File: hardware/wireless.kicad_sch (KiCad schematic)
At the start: 1 part, among them U12 ESP32-C6-MINI-1/U

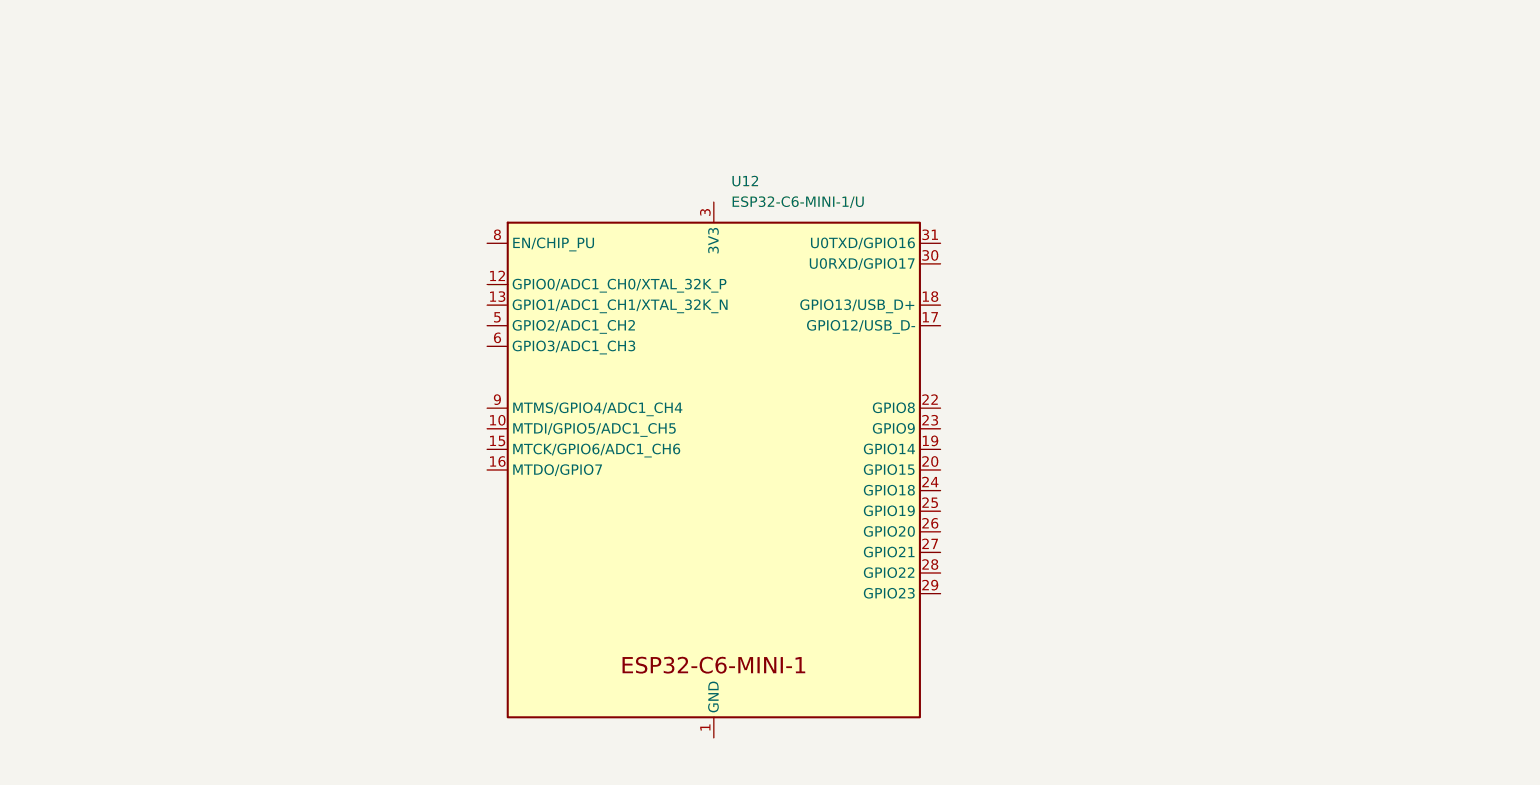
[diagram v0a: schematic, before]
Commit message: ✨ Done wireless schematic
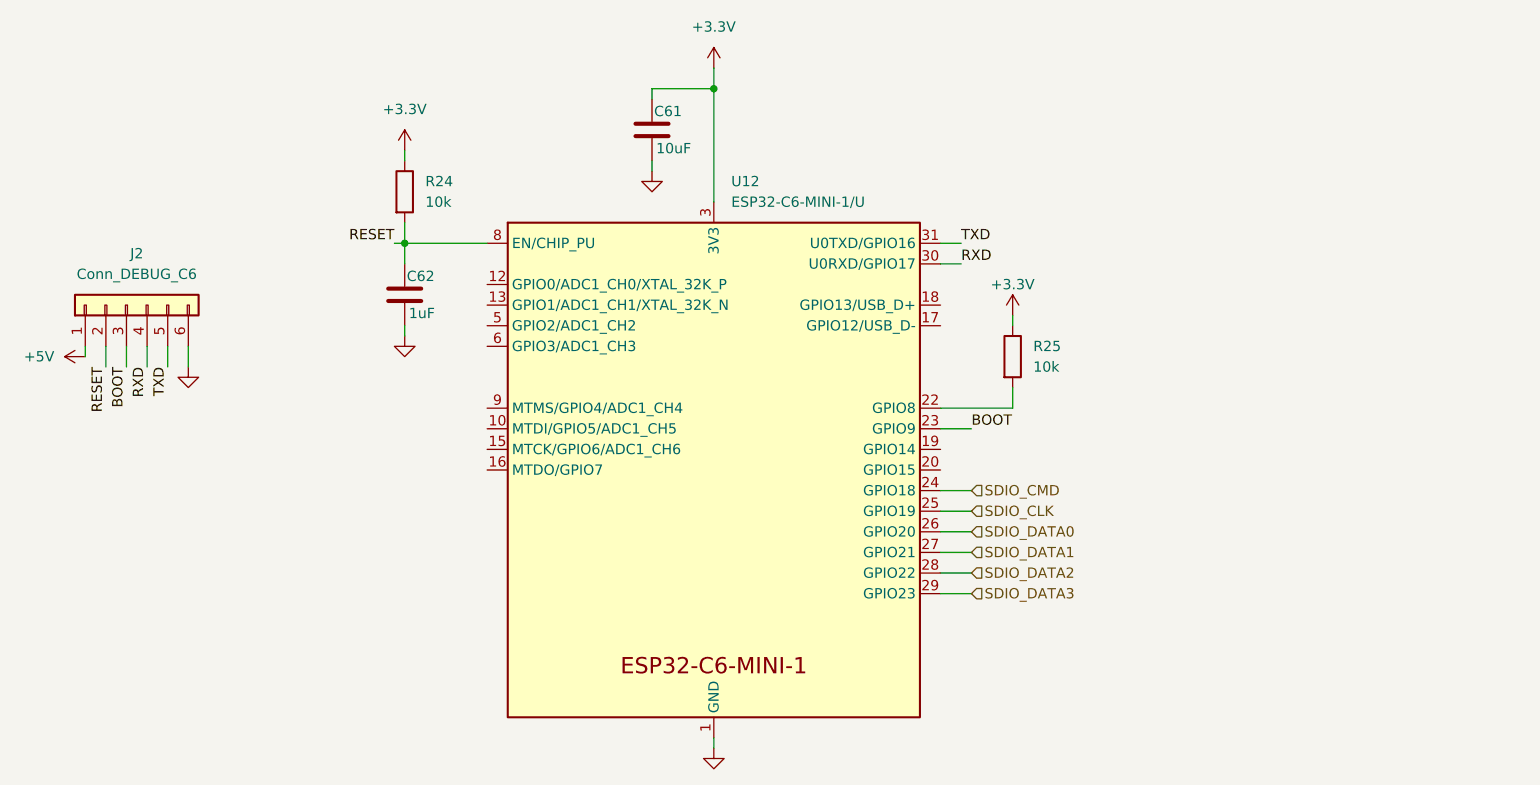
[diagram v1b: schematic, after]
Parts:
- added C61: 10uF, Capacitor_SMD:C_0805_2012Metric, symbol Device:C
- added C62: 1uF, Capacitor_SMD:C_0603_1608Metric, symbol Device:C
- added J2: Conn_DEBUG_C6, Connector_JST:JST_SHL_SM06B-SHLS-TF_1x06-1MP_P1.00mm_Horizontal, symbol Connector_Generic:Conn_01x06
- added R24, R25: 10k, PCM_Resistor_SMD_AKL:R_0603_1608Metric, symbol Device:R
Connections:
- net GND: now reaches U12.1 (GND), U12.11 (GND), U12.14 (GND), U12.2 (GND), U12.36 (GND), U12.37 (GND), U12.38 (GND), U12.39 (GND), U12.40 (GND), U12.41 (GND), U12.42 (GND), U12.43 (GND), U12.44 (GND), U12.45 (GND), U12.46 (GND), U12.47 (GND), U12.48 (GND), U12.49 (GND), U12.50 (GND), U12.51 (GND), U12.52 (GND), U12.53 (GND)
- net GND: now also C61.2, C62.2, J2.6 (Pin_6)
- net at U12.22 (GPIO8): now also R25.2
- net BOOT: now reaches U12.23 (GPIO9)
- net BOOT: now also J2.3 (Pin_3)
- net SDIO_CMD: now reaches U12.24 (GPIO18)
- net SDIO_CLK: now reaches U12.25 (GPIO19)
- net SDIO_DATA0: now reaches U12.26 (GPIO20)
- net SDIO_DATA1: now reaches U12.27 (GPIO21)
- net SDIO_DATA2: now reaches U12.28 (GPIO22)
- net SDIO_DATA3: now reaches U12.29 (GPIO23)
- net +3.3V: now reaches U12.3 (3V3)
- net +3.3V: now also C61.1, R24.1, R25.1
- net RXD: now reaches U12.30 (U0RXD/GPIO17)
- net RXD: now also J2.4 (Pin_4)
- net TXD: now reaches U12.31 (U0TXD/GPIO16)
- net TXD: now also J2.5 (Pin_5)
- net RESET: now reaches U12.8 (EN/CHIP_PU)
- net RESET: now also C62.1, J2.2 (Pin_2), R24.2
- new net +5V: J2.1 (Pin_1)

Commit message: 📂 PCB updates
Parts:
- added R30, R31, R32, R33, R34, R35: 51k, Resistor_SMD:R_0603_1608Metric, symbol Device:R
- C61: footprint Capacitor_SMD:C_0805_2012Metric -> Capacitor_SMD:C_0603_1608Metric
- R24, R25: footprint PCM_Resistor_SMD_AKL:R_0603_1608Metric -> Resistor_SMD:R_0603_1608Metric
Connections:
- net +3.3V: now also R30.2, R31.2, R32.2, R33.2, R34.2, R35.2
- net SDIO_CLK: now also R34.1
- net SDIO_CMD: now also R35.1
- net SDIO_DATA0: now also R30.1
- net SDIO_DATA1: now also R31.1
- net SDIO_DATA2: now also R32.1
- net SDIO_DATA3: now also R33.1
- net JTAG_DN: now reaches U12.17 (GPIO12/USB_D-)
- net JTAG_DN: now also J2.5 (Pin_5)
- net JTAG_DP: now reaches U12.18 (GPIO13/USB_D+)
- net JTAG_DP: now also J2.4 (Pin_4)
- net RXD: no longer names the net of U12.30 (U0RXD/GPIO17)
- net RXD: no longer J2.4 (Pin_4)
- net TXD: no longer names the net of U12.31 (U0TXD/GPIO16)
- net TXD: no longer J2.5 (Pin_5)
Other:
- moved on the sheet: R25

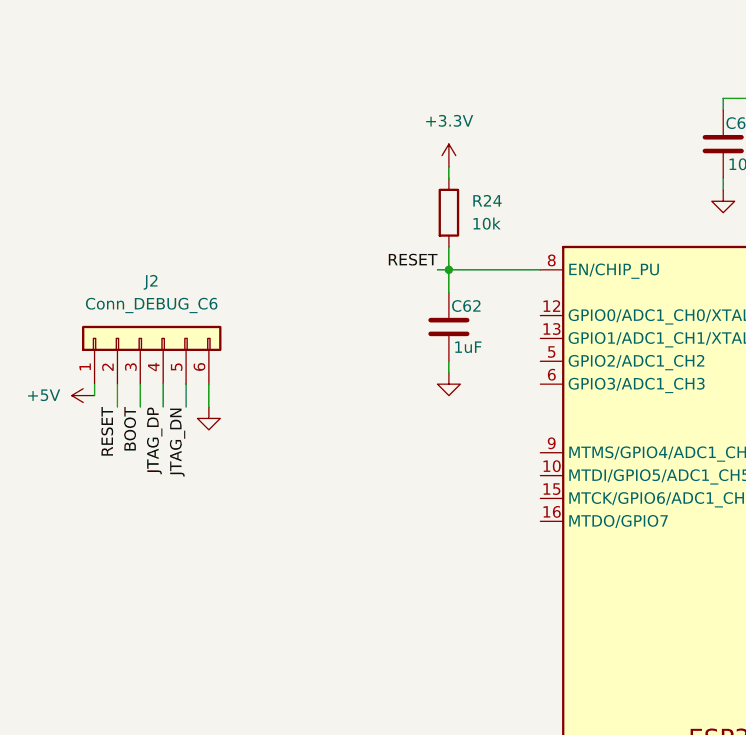
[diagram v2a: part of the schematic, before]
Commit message: 🐛 Fix errors from rev1.0
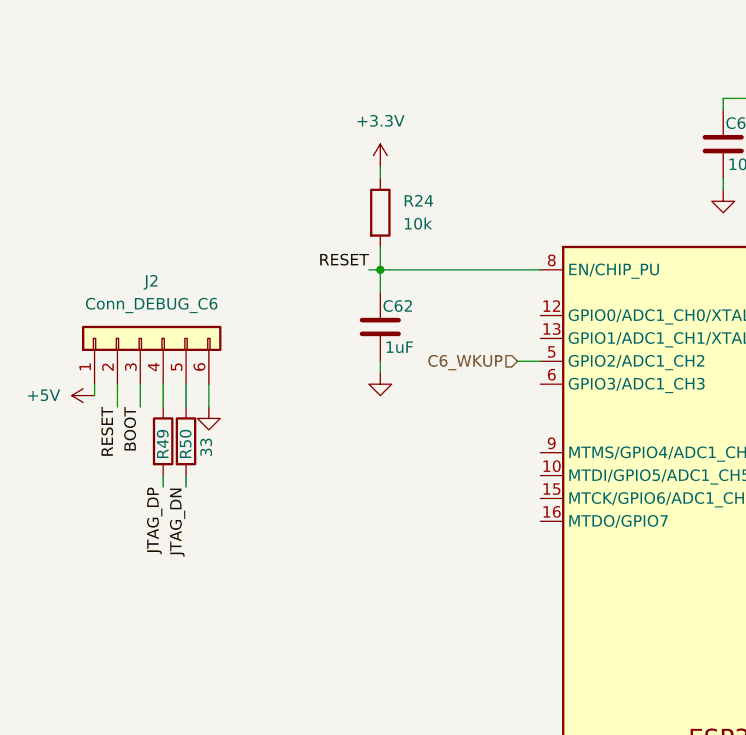
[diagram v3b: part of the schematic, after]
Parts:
- added R49, R50: 33, PCM_Resistor_SMD_AKL:R_0603_1608Metric, symbol Device:R
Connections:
- net JTAG_DN: now also R50.2; no longer J2.5 (Pin_5)
- net JTAG_DP: now also R49.2; no longer J2.4 (Pin_4)
- net C6_WKUP: now reaches U12.5 (GPIO2/ADC1_CH2)
- new net: J2.4 (Pin_4), R49.1
- new net: J2.5 (Pin_5), R50.1
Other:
- moved on the sheet: C62, R24

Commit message: ✨ Final PCB updates
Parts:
- R709: renamed from R49; footprint PCM_Resistor_SMD_AKL:R_0603_1608Metric -> PCM_Resistor_SMD_AKL:R_0402_1005Metric
- R710: renamed from R50; footprint PCM_Resistor_SMD_AKL:R_0603_1608Metric -> PCM_Resistor_SMD_AKL:R_0402_1005Metric
- renumbered C62 to C701, C61 to C702, J2 to J5, R30 to R701, R31 to R702, R32 to R703, R33 to R704, R34 to R705, R35 to R706, R24 to R707, R25 to R708, U12 to U3
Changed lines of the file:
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@@
 		(on_board yes)
 		(dnp no)
-		(property "Reference" "R35"
+		(property "Reference" "R706"
 			(at 237.49 95.25 90)
 			(effects
@@
 			(project "peak"
 				(path "/54a54a18-4a65-4728-b17a-32b4a97370c1/4b2e3f36-15b2-4931-8779-b46f5157a5a6"
-					(reference "R35")
+					(reference "R706")
 					(unit 1)
 				)
@@
 		(on_board yes)
 		(dnp no)
-		(property "Reference" "C61"
+		(property "Reference" "C702"
 			(at 151.384 49.784 0)
 			(effects
@@
 			(project ""
 				(path "/54a54a18-4a65-4728-b17a-32b4a97370c1/4b2e3f36-15b2-4931-8779-b46f5157a5a6"
-					(reference "C61")
+					(reference "C702")
 					(unit 1)
 				)
@@
 		(on_board yes)
 		(dnp no)
-		(property "Reference" "R32"
+		(property "Reference" "R703"
 			(at 237.49 87.63 90)
 			(effects
@@
 			(project "peak"
 				(path "/54a54a18-4a65-4728-b17a-32b4a97370c1/4b2e3f36-15b2-4931-8779-b46f5157a5a6"
-					(reference "R32")
+					(reference "R703")
 					(unit 1)
 				)
@@
 		(dnp no)
 		(fields_autoplaced yes)
-		(property "Reference" "#PWR097"
+		(property "Reference" "#PWR0216"
 			(at 158.75 48.26 0)
 			(effects
@@
 			(project ""
 				(path "/54a54a18-4a65-4728-b17a-32b4a97370c1/4b2e3f36-15b2-4931-8779-b46f5157a5a6"
-					(reference "#PWR097")
+					(reference "#PWR0216")
 					(unit 1)
 				)
@@
 		(dnp no)
 		(fields_autoplaced yes)
-		(property "Reference" "#PWR099"
+		(property "Reference" "#PWR0210"
 			(at 113.03 58.42 0)
 			(effects
@@
 			(project "peak"
 				(path "/54a54a18-4a65-4728-b17a-32b4a97370c1/4b2e3f36-15b2-4931-8779-b46f5157a5a6"
-					(reference "#PWR099")
+					(reference "#PWR0210")
 					(unit 1)
 				)
@@
 		(dnp no)
 		(fields_autoplaced yes)
-		(property "Reference" "#PWR0100"
+		(property "Reference" "#PWR0208"
 			(at 113.03 83.82 0)
 			(effects
@@
 			(project "peak"
 				(path "/54a54a18-4a65-4728-b17a-32b4a97370c1/4b2e3f36-15b2-4931-8779-b46f5157a5a6"
-					(reference "#PWR0100")
+					(reference "#PWR0208")
 					(unit 1)
 				)
@@
 		(dnp no)
 		(fields_autoplaced yes)
-		(property "Reference" "#PWR0105"
+		(property "Reference" "#PWR0212"
 			(at 243.84 88.9 0)
 			(effects
@@
 			(project "peak"
 				(path "/54a54a18-4a65-4728-b17a-32b4a97370c1/4b2e3f36-15b2-4931-8779-b46f5157a5a6"
-					(reference "#PWR0105")
+					(reference "#PWR0212")
 					(unit 1)
 				)
@@
 		(dnp no)
 		(fields_autoplaced yes)
-		(property "Reference" "J2"
+		(property "Reference" "J5"
 			(at 87.63 67.31 90)
 			(effects
@@
 			(project ""
 				(path "/54a54a18-4a65-4728-b17a-32b4a97370c1/4b2e3f36-15b2-4931-8779-b46f5157a5a6"
-					(reference "J2")
+					(reference "J5")
 					(unit 1)
 				)
@@
 		(on_board yes)
 		(dnp no)
-		(property "Reference" "R31"
+		(property "Reference" "R702"
 			(at 237.49 85.09 90)
 			(effects
@@
 			(project "peak"
 				(path "/54a54a18-4a65-4728-b17a-32b4a97370c1/4b2e3f36-15b2-4931-8779-b46f5157a5a6"
-					(reference "R31")
+					(reference "R702")
 					(unit 1)
 				)
@@
 		(on_board yes)
 		(dnp no)
-		(property "Reference" "C62"
+		(property "Reference" "C701"
 			(at 113.284 70.104 0)
 			(effects
@@
 			(project "peak"
 				(path "/54a54a18-4a65-4728-b17a-32b4a97370c1/4b2e3f36-15b2-4931-8779-b46f5157a5a6"
-					(reference "C62")
+					(reference "C701")
 					(unit 1)
 				)
@@
 		(on_board yes)
 		(dnp no)
-		(property "Reference" "R33"
+		(property "Reference" "R704"
 			(at 237.49 90.17 90)
 			(effects
@@
 			(project "peak"
 				(path "/54a54a18-4a65-4728-b17a-32b4a97370c1/4b2e3f36-15b2-4931-8779-b46f5157a5a6"
-					(reference "R33")
+					(reference "R704")
 					(unit 1)
 				)
@@
 		(dnp no)
 		(fields_autoplaced yes)
-		(property "Reference" "#PWR0102"
+		(property "Reference" "#PWR0209"
 			(at 85.09 80.01 0)
 			(effects
@@
 			(project ""
 				(path "/54a54a18-4a65-4728-b17a-32b4a97370c1/4b2e3f36-15b2-4931-8779-b46f5157a5a6"
-					(reference "#PWR0102")
+					(reference "#PWR0209")
 					(unit 1)
 				)
@@
 		(dnp no)
 		(fields_autoplaced yes)
-		(property "Reference" "R25"
+		(property "Reference" "R708"
 			(at 209.55 78.7399 0)
 			(effects
@@
 			(project "peak"
 				(path "/54a54a18-4a65-4728-b17a-32b4a97370c1/4b2e3f36-15b2-4931-8779-b46f5157a5a6"
-					(reference "R25")
+					(reference "R708")
 					(unit 1)
 				)
@@
 		(dnp no)
 		(fields_autoplaced yes)
-		(property "Reference" "R24"
+		(property "Reference" "R707"
 			(at 115.57 58.4199 0)
 			(effects
@@
 			(project ""
 				(path "/54a54a18-4a65-4728-b17a-32b4a97370c1/4b2e3f36-15b2-4931-8779-b46f5157a5a6"
-					(reference "R24")
+					(reference "R707")
 					(unit 1)
 				)
@@
 		(dnp no)
 		(fields_autoplaced yes)
-		(property "Reference" "U12"
+		(property "Reference" "U3"
 			(at 160.8933 58.42 0)
 			(effects
@@
 			(project ""
 				(path "/54a54a18-4a65-4728-b17a-32b4a97370c1/4b2e3f36-15b2-4931-8779-b46f5157a5a6"
-					(reference "U12")
+					(reference "U3")
 					(unit 1)
 				)
@@
 		(dnp no)
 		(fields_autoplaced yes)
-		(property "Reference" "#PWR096"
+		(property "Reference" "#PWR0215"
 			(at 151.13 63.5 0)
 			(effects
@@
 			(project ""
 				(path "/54a54a18-4a65-4728-b17a-32b4a97370c1/4b2e3f36-15b2-4931-8779-b46f5157a5a6"
-					(reference "#PWR096")
+					(reference "#PWR0215")
 					(unit 1)
 				)
@@
 		(on_board yes)
 		(dnp no)
-		(property "Reference" "R30"
+		(property "Reference" "R701"
 			(at 237.49 82.55 90)
 			(effects
@@
 			(project "peak"
 				(path "/54a54a18-4a65-4728-b17a-32b4a97370c1/4b2e3f36-15b2-4931-8779-b46f5157a5a6"
-					(reference "R30")
+					(reference "R701")
 					(unit 1)
 				)
@@
 		(on_board yes)
 		(dnp no)
-		(property "Reference" "R49"
+		(property "Reference" "R709"
 			(at 88.9 87.122 90)
 			(effects
@@
 			)
 		)
-		(property "Footprint" "PCM_Resistor_SMD_AKL:R_0603_1608Metric"
+		(property "Footprint" "PCM_Resistor_SMD_AKL:R_0402_1005Metric"
 			(at 87.122 85.09 90)
 			(effects
@@
 			(project "peak"
 				(path "/54a54a18-4a65-4728-b17a-32b4a97370c1/4b2e3f36-15b2-4931-8779-b46f5157a5a6"
-					(reference "R49")
+					(reference "R709")
 					(unit 1)
 				)
@@
 		(dnp no)
 		(fields_autoplaced yes)
-		(property "Reference" "#PWR0103"
+		(property "Reference" "#PWR0211"
 			(at 93.98 87.63 0)
 			(effects
@@
 			(project "peak"
 				(path "/54a54a18-4a65-4728-b17a-32b4a97370c1/4b2e3f36-15b2-4931-8779-b46f5157a5a6"
-					(reference "#PWR0103")
+					(reference "#PWR0211")
 					(unit 1)
 				)
@@
 		(dnp no)
 		(fields_autoplaced yes)
-		(property "Reference" "#PWR098"
+		(property "Reference" "#PWR0214"
 			(at 158.75 134.62 0)
 			(effects
@@
 			(project "peak"
 				(path "/54a54a18-4a65-4728-b17a-32b4a97370c1/4b2e3f36-15b2-4931-8779-b46f5157a5a6"
-					(reference "#PWR098")
+					(reference "#PWR0214")
 					(unit 1)
 				)
@@
 		(on_board yes)
 		(dnp no)
-		(property "Reference" "#PWR0101"
+		(property "Reference" "#PWR0213"
 			(at 207.01 78.74 0)
 			(effects
@@
 			(project "peak"
 				(path "/54a54a18-4a65-4728-b17a-32b4a97370c1/4b2e3f36-15b2-4931-8779-b46f5157a5a6"
-					(reference "#PWR0101")
+					(reference "#PWR0213")
 					(unit 1)
 				)
@@
 		(on_board yes)
 		(dnp no)
-		(property "Reference" "R34"
+		(property "Reference" "R705"
 			(at 237.49 92.71 90)
 			(effects
@@
 			(project "peak"
 				(path "/54a54a18-4a65-4728-b17a-32b4a97370c1/4b2e3f36-15b2-4931-8779-b46f5157a5a6"
-					(reference "R34")
+					(reference "R705")
 					(unit 1)
 				)
@@
 		(on_board yes)
 		(dnp no)
-		(property "Reference" "R50"
+		(property "Reference" "R710"
 			(at 91.44 87.122 90)
 			(effects
@@
 			)
 		)
-		(property "Footprint" "PCM_Resistor_SMD_AKL:R_0603_1608Metric"
+		(property "Footprint" "PCM_Resistor_SMD_AKL:R_0402_1005Metric"
 			(at 89.662 85.09 90)
 			(effects
@@
 			(project "peak"
 				(path "/54a54a18-4a65-4728-b17a-32b4a97370c1/4b2e3f36-15b2-4931-8779-b46f5157a5a6"
-					(reference "R50")
-					(unit 1)
-				)
+					(reference "R710")
+					(unit 1)
+				)
